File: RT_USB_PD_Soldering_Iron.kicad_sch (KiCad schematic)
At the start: 64 parts, among them J1 USB4105-GF-A, J2 35RASMT4BHNTRX, J3 Conn_02x03_Odd_Even, SW1 SW_Push, SW2 SW_Push, U1 SPX3819M5-L-3-3, U2 ECMF02-AMX6, U3 FUSB302BMPX, U4 STM32G431Kxxx, U5 TPS25982ONRGET, U6 BMI270, U7 OPA376AIDCKR

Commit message: Change mounting holes to Plated Through Holes
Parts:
- H1, H2: footprint MountingHole:MountingHole_2.2mm_M2_ISO7380 -> local:MountingHole_2.2mm_M2_ISO7380_Pad; symbol Mechanical:MountingHole -> Mechanical:MountingHole_Pad
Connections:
- net GND: now also H1.1, H2.1
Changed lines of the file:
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@@
+    (stroke (width 0) (type solid) (color 0 0 0 0))
+  )
+  (wire (pts (xy 158.75 69.85) (xy 158.75 71.12))
     (stroke (width 0) (type solid) (color 0 0 0 0))
   )
@@
     )
   )
+  (symbol (lib_id "power:GND") (at 158.75 59.69 0) (unit 1)
+    (in_bom yes) (on_board yes)
+    (property "Reference" "#PWR0101" (id 0) (at 158.75 66.04 0)
+      (effects (font (size 1.27 1.27)) hide)
+    )
+    (property "Value" "GND" (id 1) (at 158.75 63.5 0))
+    (property "Footprint" "" (id 2) (at 158.75 59.69 0)
+      (effects (font (size 1.27 1.27)) hide)
+    )
+    (property "Datasheet" "" (id 3) (at 158.75 59.69 0)
+      (effects (font (size 1.27 1.27)) hide)
+    )
+  )
+  (symbol (lib_id "power:GND") (at 158.75 71.12 0) (unit 1)
+    (in_bom yes) (on_board yes)
+    (property "Reference" "#PWR0102" (id 0) (at 158.75 77.47 0)
+      (effects (font (size 1.27 1.27)) hide)
+    )
+    (property "Value" "GND" (id 1) (at 158.75 74.93 0))
+    (property "Footprint" "" (id 2) (at 158.75 71.12 0)
+      (effects (font (size 1.27 1.27)) hide)
+    )
+    (property "Datasheet" "" (id 3) (at 158.75 71.12 0)
+      (effects (font (size 1.27 1.27)) hide)
+    )
+  )
   (symbol (lib_id "power:GND") (at 163.83 35.56 0) (unit 1)
     (in_bom yes) (on_board yes)
@@
     )
     (property "Datasheet" "" (id 3) (at 271.78 90.17 0)
-      (effects (font (size 1.27 1.27)) hide)
-    )
-  )
-  (symbol (lib_id "Mechanical:MountingHole") (at 158.75 62.23 0) (unit 1)
-    (in_bom yes) (on_board yes)
-    (property "Reference" "H1" (id 0) (at 162.56 60.96 0)
-      (effects (font (size 1.27 1.27)) (justify left))
-    )
-    (property "Value" "MountingHole" (id 1) (at 162.56 62.23 0)
-      (effects (font (size 1.27 1.27)) (justify left))
-    )
-    (property "Footprint" "MountingHole:MountingHole_2.2mm_M2_ISO7380" (id 2) (at 158.75 62.23 0)
-      (effects (font (size 1.27 1.27)) hide)
-    )
-    (property "Datasheet" "~" (id 3) (at 158.75 62.23 0)
-      (effects (font (size 1.27 1.27)) hide)
-    )
-  )
-  (symbol (lib_id "Mechanical:MountingHole") (at 158.75 67.31 0) (unit 1)
-    (in_bom yes) (on_board yes)
-    (property "Reference" "H2" (id 0) (at 162.56 66.04 0)
-      (effects (font (size 1.27 1.27)) (justify left))
-    )
-    (property "Value" "MountingHole" (id 1) (at 162.56 67.31 0)
-      (effects (font (size 1.27 1.27)) (justify left))
-    )
-    (property "Footprint" "MountingHole:MountingHole_2.2mm_M2_ISO7380" (id 2) (at 158.75 67.31 0)
-      (effects (font (size 1.27 1.27)) hide)
-    )
-    (property "Datasheet" "~" (id 3) (at 158.75 67.31 0)
       (effects (font (size 1.27 1.27)) hide)
     )
@@
     )
     (property "Tolerance" "5%" (id 4) (at 243.84 59.69 90))
+  )
+  (symbol (lib_id "Mechanical:MountingHole_Pad") (at 158.75 57.15 0) (unit 1)
+    (in_bom yes) (on_board yes)
+    (property "Reference" "H1" (id 0) (at 162.56 55.88 0)
+      (effects (font (size 1.27 1.27)) (justify left))
+    )
+    (property "Value" "MountingHole" (id 1) (at 162.56 57.15 0)
+      (effects (font (size 1.27 1.27)) (justify left))
+    )
+    (property "Footprint" "local:MountingHole_2.2mm_M2_ISO7380_Pad" (id 2) (at 158.75 57.15 0)
+      (effects (font (size 1.27 1.27)) hide)
+    )
+    (property "Datasheet" "" (id 3) (at 158.75 57.15 0)
+      (effects (font (size 1.27 1.27)) hide)
+    )
+  )
+  (symbol (lib_id "Mechanical:MountingHole_Pad") (at 158.75 67.31 0) (unit 1)
+    (in_bom yes) (on_board yes)
+    (property "Reference" "H2" (id 0) (at 162.56 66.04 0)
+      (effects (font (size 1.27 1.27)) (justify left))
+    )
+    (property "Value" "MountingHole" (id 1) (at 162.56 67.31 0)
+      (effects (font (size 1.27 1.27)) (justify left))
+    )
+    (property "Footprint" "local:MountingHole_2.2mm_M2_ISO7380_Pad" (id 2) (at 158.75 67.31 0)
+      (effects (font (size 1.27 1.27)) hide)
+    )
+    (property "Datasheet" "" (id 3) (at 158.75 67.31 0)
+      (effects (font (size 1.27 1.27)) hide)
+    )
   )
   (symbol (lib_id "Device:D_TVS") (at 39.37 127 90) (unit 1)
@@
       (reference "#PWR049") (unit 1) (value "GND") (footprint "")
     )
+    (path "/43d7f25b-5f64-4d58-b045-15bcb5e20473"
+      (reference "#PWR0101") (unit 1) (value "GND") (footprint "")
+    )
+    (path "/2d259d26-c2b5-4277-a66e-8e8e14182bb9"
+      (reference "#PWR0102") (unit 1) (value "GND") (footprint "")
+    )
     (path "/43030675-5e71-43da-8ffb-a16ee19b5a30"
       (reference "C1") (unit 1) (value "10uF 35v") (footprint "Capacitor_SMD:C_0603_1608Metric_Pad1.05x0.95mm_HandSolder")
@@
     )
     (path "/ffc9b8c7-d039-4169-9ffd-a8a17d23ff13"
-      (reference "H1") (unit 1) (value "MountingHole") (footprint "MountingHole:MountingHole_2.2mm_M2_ISO7380")
+      (reference "H1") (unit 1) (value "MountingHole") (footprint "local:MountingHole_2.2mm_M2_ISO7380_Pad")
     )
     (path "/54ec1b8d-8ea6-48ad-b832-ec785bd67a48"
-      (reference "H2") (unit 1) (value "MountingHole") (footprint "MountingHole:MountingHole_2.2mm_M2_ISO7380")
+      (reference "H2") (unit 1) (value "MountingHole") (footprint "local:MountingHole_2.2mm_M2_ISO7380_Pad")
     )
     (path "/a9b433d3-f6a8-447d-add7-160962cdce04"

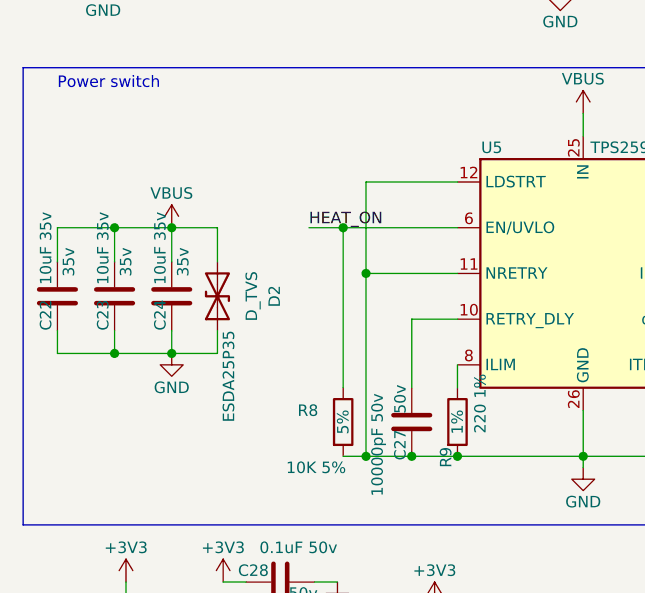
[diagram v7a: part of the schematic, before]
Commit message: Final tweaks before sending to Fab, fix diode D2 orientation
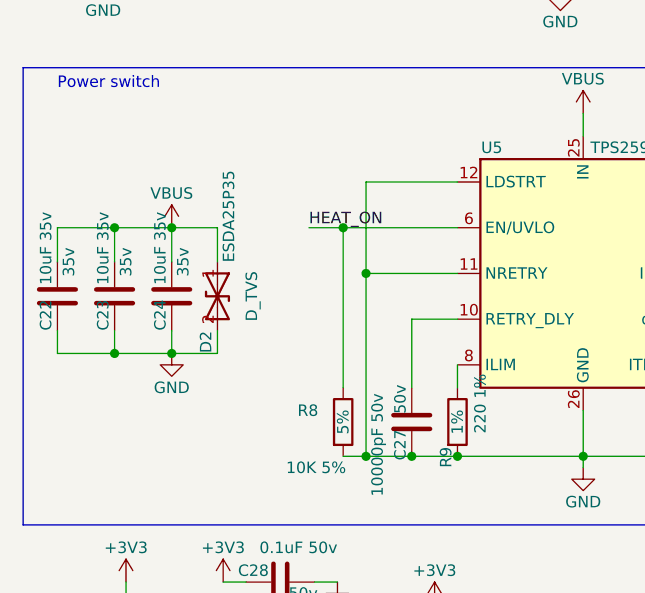
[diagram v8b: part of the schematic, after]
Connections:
- net GND: now also D2.2 (A2); no longer D2.1 (A1)
- net IN: now also D2.1 (A1); no longer D2.2 (A2)
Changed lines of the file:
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@@
     )
-  )
-  (symbol (lib_id "Device:D_TVS") (at 39.37 127 90) (unit 1)
-    (in_bom yes) (on_board yes)
-    (property "Reference" "D2" (id 0) (at 45.72 127 0))
-    (property "Value" "D_TVS" (id 1) (at 43.18 127 0))
-    (property "Footprint" "D_1610:D_1610" (id 2) (at 39.37 127 0)
-      (effects (font (size 1.27 1.27)) hide)
-    )
-    (property "Datasheet" "~" (id 3) (at 39.37 127 0)
-      (effects (font (size 1.27 1.27)) hide)
-    )
-    (property "Part" "ESDA25P35" (id 4) (at 40.64 135.89 0))
   )
   (symbol (lib_id "Device:D_Schottky") (at 119.38 119.38 270) (unit 1)
@@
     (property "Part" "SDM2U30CSP-7" (id 4) (at 123.19 121.92 90))
   )
+  (symbol (lib_id "Device:D_TVS") (at 39.37 127 270) (unit 1)
+    (in_bom yes) (on_board yes)
+    (property "Reference" "D2" (id 0) (at 38.1 132.08 0))
+    (property "Value" "D_TVS" (id 1) (at 43.18 127 0))
+    (property "Footprint" "D_1610:D_1610" (id 2) (at 39.37 127 0)
+      (effects (font (size 1.27 1.27)) hide)
+    )
+    (property "Datasheet" "~" (id 3) (at 39.37 127 0)
+      (effects (font (size 1.27 1.27)) hide)
+    )
+    (property "Part" "ESDA25P35" (id 4) (at 40.64 118.11 0))
+  )
   (symbol (lib_id "Device:C") (at 21.59 127 0) (unit 1)
